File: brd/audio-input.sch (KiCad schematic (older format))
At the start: 15 parts, among them U6 MCP6004

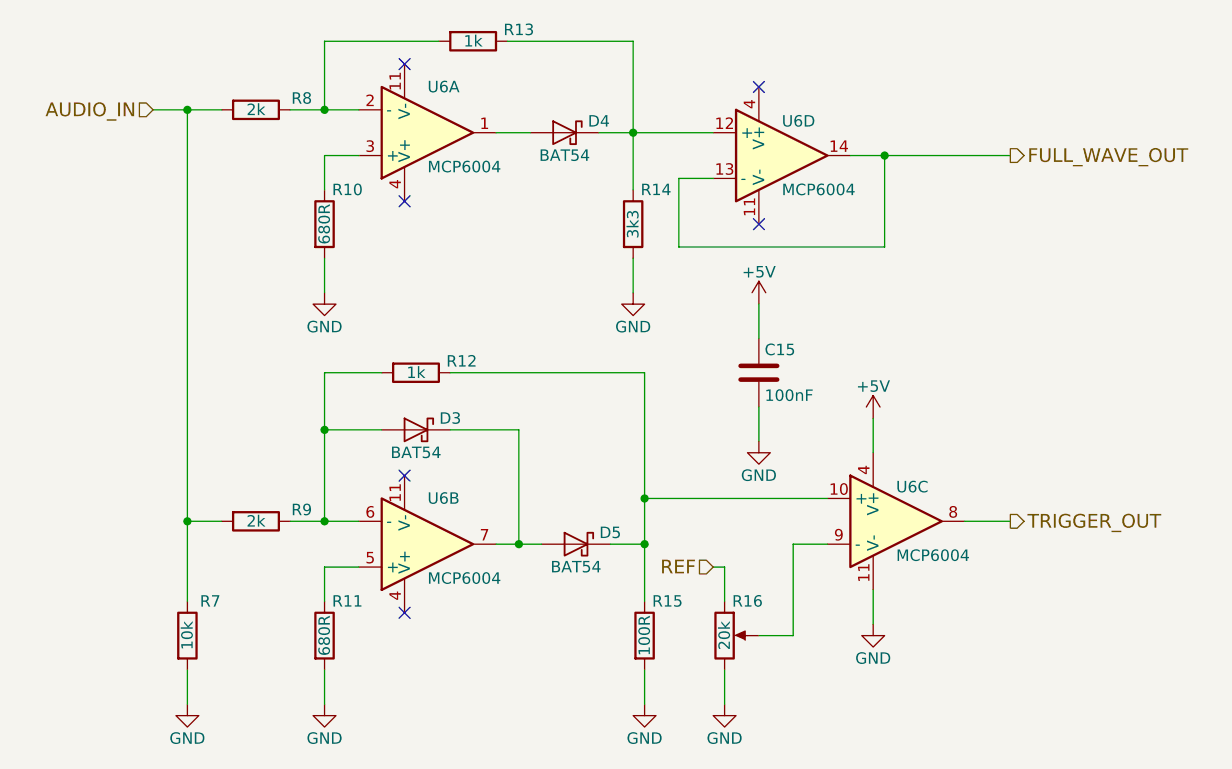
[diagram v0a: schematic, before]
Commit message: corregido problema con referencia analogica
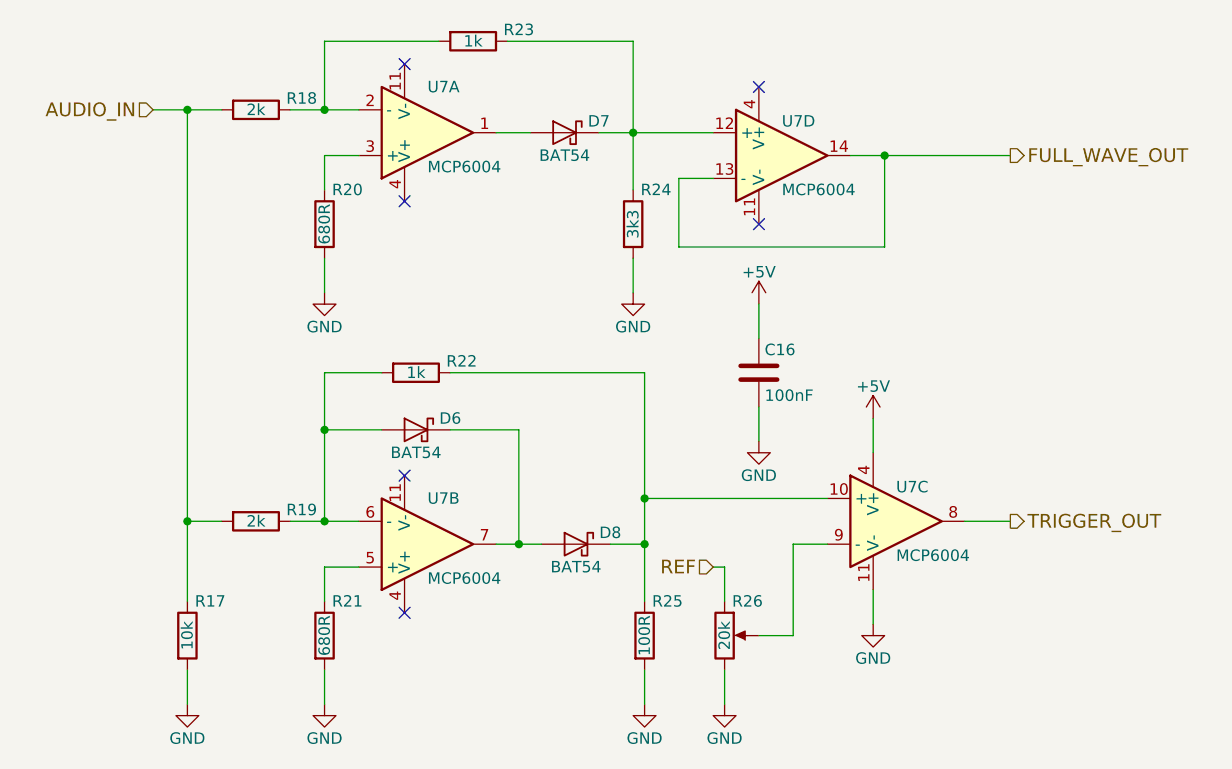
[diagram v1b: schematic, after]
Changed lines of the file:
@@
 AR Path="/5DA48168/5DA48258" Ref="U6"  Part="2"
 AR Path="/5DA4FC1E/5DA48258" Ref="U7"  Part="2"
-F 0 "U6" H 5050 4050 50  0000 L CNN
+F 0 "U7" H 5050 4050 50  0000 L CNN
 F 1 "MCP6004" H 5050 4400 50  0000 L CNN
 F 2 "Housings_SSOP:TSSOP-14_4.4x5mm_Pitch0.65mm" H 5000 4350 50  0001 C CNN
@@
 AR Path="/5DA48168/5DA482D7" Ref="R11"  Part="1"
 AR Path="/5DA4FC1E/5DA482D7" Ref="R21"  Part="1"
-F 0 "R11" H 4700 4800 50  0000 C CNN
+F 0 "R21" H 4700 4800 50  0000 C CNN
 F 1 "680R" V 4600 4650 50  0000 C CNN
 F 2 "Resistors_SMD:R_0805_HandSoldering" V 4530 4650 50  0001 C CNN
@@
 AR Path="/5DA48168/5DA48CC8" Ref="R15"  Part="1"
 AR Path="/5DA4FC1E/5DA48CC8" Ref="R25"  Part="1"
-F 0 "R15" H 6100 4800 50  0000 C CNN
+F 0 "R25" H 6100 4800 50  0000 C CNN
 F 1 "100R" V 6000 4650 50  0000 C CNN
 F 2 "Resistors_SMD:R_0805_HandSoldering" V 5930 4650 50  0001 C CNN
@@
 AR Path="/5DA48168/5DA48D92" Ref="R9"  Part="1"
 AR Path="/5DA4FC1E/5DA48D92" Ref="R19"  Part="1"
-F 0 "R9" V 4250 4350 50  0000 C CNN
+F 0 "R19" V 4250 4350 50  0000 C CNN
 F 1 "2k" V 4300 4150 50  0000 C CNN
 F 2 "Resistors_SMD:R_0805_HandSoldering" V 4230 4150 50  0001 C CNN
@@
 AR Path="/5DA48168/5DA48DF2" Ref="R12"  Part="1"
 AR Path="/5DA4FC1E/5DA48DF2" Ref="R22"  Part="1"
-F 0 "R12" V 4950 3700 50  0000 C CNN
+F 0 "R22" V 4950 3700 50  0000 C CNN
 F 1 "1k" V 5000 3500 50  0000 C CNN
 F 2 "Resistors_SMD:R_0805_HandSoldering" V 4930 3500 50  0001 C CNN
@@
 AR Path="/5DA48168/5DA49319" Ref="R7"  Part="1"
 AR Path="/5DA4FC1E/5DA49319" Ref="R17"  Part="1"
-F 0 "R7" H 4100 4800 50  0000 C CNN
+F 0 "R17" H 4100 4800 50  0000 C CNN
 F 1 "10k" V 4000 4650 50  0000 C CNN
 F 2 "Resistors_SMD:R_0805_HandSoldering" V 3930 4650 50  0001 C CNN
@@
 AR Path="/5DA48168/5DA496BC" Ref="U6"  Part="1"
 AR Path="/5DA4FC1E/5DA496BC" Ref="U7"  Part="1"
-F 0 "U6" H 5050 2250 50  0000 L CNN
+F 0 "U7" H 5050 2250 50  0000 L CNN
 F 1 "MCP6004" H 5050 2600 50  0000 L CNN
 F 2 "Housings_SSOP:TSSOP-14_4.4x5mm_Pitch0.65mm" H 5000 2550 50  0001 C CNN
@@
 AR Path="/5DA48168/5DA496C2" Ref="R10"  Part="1"
 AR Path="/5DA4FC1E/5DA496C2" Ref="R20"  Part="1"
-F 0 "R10" H 4700 3000 50  0000 C CNN
+F 0 "R20" H 4700 3000 50  0000 C CNN
 F 1 "680R" V 4600 2850 50  0000 C CNN
 F 2 "Resistors_SMD:R_0805_HandSoldering" V 4530 2850 50  0001 C CNN
@@
 AR Path="/5DA48168/5DA496C8" Ref="D4"  Part="1"
 AR Path="/5DA4FC1E/5DA496C8" Ref="D7"  Part="1"
-F 0 "D4" H 5500 2500 50  0000 C CNN
+F 0 "D7" H 5500 2500 50  0000 C CNN
 F 1 "BAT54" H 5650 2350 50  0000 C CNN
 F 2 "Diodes_SMD:D_SOD-123" H 5650 2450 50  0001 C CNN
@@
 AR Path="/5DA48168/5DA496D0" Ref="R14"  Part="1"
 AR Path="/5DA4FC1E/5DA496D0" Ref="R24"  Part="1"
-F 0 "R14" H 6050 3000 50  0000 C CNN
+F 0 "R24" H 6050 3000 50  0000 C CNN
 F 1 "3k3" V 5950 2850 50  0000 C CNN
 F 2 "Resistors_SMD:R_0805_HandSoldering" V 5880 2850 50  0001 C CNN
@@
 AR Path="/5DA48168/5DA496D6" Ref="R8"  Part="1"
 AR Path="/5DA4FC1E/5DA496D6" Ref="R18"  Part="1"
-F 0 "R8" V 4250 2550 50  0000 C CNN
+F 0 "R18" V 4250 2550 50  0000 C CNN
 F 1 "2k" V 4300 2350 50  0000 C CNN
 F 2 "Resistors_SMD:R_0805_HandSoldering" V 4230 2350 50  0001 C CNN
@@
 AR Path="/5DA48168/5DA496DC" Ref="R13"  Part="1"
 AR Path="/5DA4FC1E/5DA496DC" Ref="R23"  Part="1"
-F 0 "R13" V 5200 2250 50  0000 C CNN
+F 0 "R23" V 5200 2250 50  0000 C CNN
 F 1 "1k" V 5250 2050 50  0000 C CNN
 F 2 "Resistors_SMD:R_0805_HandSoldering" V 5180 2050 50  0001 C CNN
@@
 Connection ~ 4600 2350
 $Comp
-L GND #PWR043
+L GND #PWR47
 U 1 1 5DA49A66
 P 6000 4950
-AR Path="/5DA48168/5DA49A66" Ref="#PWR043"  Part="1"
-AR Path="/5DA4FC1E/5DA49A66" Ref="#PWR053"  Part="1"
-F 0 "#PWR043" H 6000 4700 50  0001 C CNN
+AR Path="/5DA48168/5DA49A66" Ref="#PWR47"  Part="1"
+AR Path="/5DA4FC1E/5DA49A66" Ref="#PWR57"  Part="1"
+F 0 "#PWR57" H 6000 4700 50  0001 C CNN
 F 1 "GND" H 6000 4800 50  0000 C CNN
 F 2 "" H 6000 4950 50  0001 C CNN
@@
 $EndComp
 $Comp
-L GND #PWR044
+L GND #PWR45
 U 1 1 5DA49B2E
 P 4600 4950
-AR Path="/5DA48168/5DA49B2E" Ref="#PWR044"  Part="1"
-AR Path="/5DA4FC1E/5DA49B2E" Ref="#PWR054"  Part="1"
-F 0 "#PWR044" H 4600 4700 50  0001 C CNN
+AR Path="/5DA48168/5DA49B2E" Ref="#PWR45"  Part="1"
+AR Path="/5DA4FC1E/5DA49B2E" Ref="#PWR55"  Part="1"
+F 0 "#PWR55" H 4600 4700 50  0001 C CNN
 F 1 "GND" H 4600 4800 50  0000 C CNN
 F 2 "" H 4600 4950 50  0001 C CNN
@@
 AR Path="/5DA48168/5DA49C44" Ref="U6"  Part="3"
 AR Path="/5DA4FC1E/5DA49C44" Ref="U7"  Part="3"
-F 0 "U6" H 7100 4300 50  0000 L CNN
+F 0 "U7" H 7100 4300 50  0000 L CNN
 F 1 "MCP6004" H 7100 4000 50  0000 L CNN
 F 2 "Housings_SSOP:TSSOP-14_4.4x5mm_Pitch0.65mm" H 7050 4250 50  0001 C CNN
@@
 AR Path="/5DA48168/5DA49DEC" Ref="R16"  Part="1"
 AR Path="/5DA4FC1E/5DA49DEC" Ref="R26"  Part="1"
-F 0 "R16" H 6450 4800 50  0000 C CNN
+F 0 "R26" H 6450 4800 50  0000 C CNN
 F 1 "20k" V 6350 4650 50  0000 C CNN
 F 2 "Potentiometers:Potentiometer_Trimmer_Bourns_3299P" H 6350 4650 50  0001 C CNN
@@
 $EndComp
 $Comp
-L GND #PWR045
+L GND #PWR52
 U 1 1 5DA49F10
 P 7000 4600
-AR Path="/5DA48168/5DA49F10" Ref="#PWR045"  Part="1"
-AR Path="/5DA4FC1E/5DA49F10" Ref="#PWR055"  Part="1"
-F 0 "#PWR045" H 7000 4350 50  0001 C CNN
+AR Path="/5DA48168/5DA49F10" Ref="#PWR52"  Part="1"
+AR Path="/5DA4FC1E/5DA49F10" Ref="#PWR62"  Part="1"
+F 0 "#PWR62" H 7000 4350 50  0001 C CNN
 F 1 "GND" H 7000 4450 50  0000 C CNN
 F 2 "" H 7000 4600 50  0001 C CNN
@@
 $EndComp
 $Comp
-L +5V #PWR046
+L +5V #PWR49
 U 1 1 5DA49F3D
 P 6500 3200
-AR Path="/5DA48168/5DA49F3D" Ref="#PWR046"  Part="1"
-AR Path="/5DA4FC1E/5DA49F3D" Ref="#PWR056"  Part="1"
-F 0 "#PWR046" H 6500 3050 50  0001 C CNN
+AR Path="/5DA48168/5DA49F3D" Ref="#PWR49"  Part="1"
+AR Path="/5DA4FC1E/5DA49F3D" Ref="#PWR59"  Part="1"
+F 0 "#PWR59" H 6500 3050 50  0001 C CNN
 F 1 "+5V" H 6500 3340 50  0000 C CNN
 F 2 "" H 6500 3200 50  0001 C CNN
@@
 AR Path="/5DA48168/5DA4A24A" Ref="U6"  Part="4"
 AR Path="/5DA4FC1E/5DA4A24A" Ref="U7"  Part="4"
-F 0 "U6" H 6600 2700 50  0000 L CNN
+F 0 "U7" H 6600 2700 50  0000 L CNN
 F 1 "MCP6004" H 6600 2400 50  0000 L CNN
 F 2 "Housings_SSOP:TSSOP-14_4.4x5mm_Pitch0.65mm" H 6550 2650 50  0001 C CNN
@@
 	6900 2550 7600 2550
 $Comp
-L GND #PWR047
+L GND #PWR46
 U 1 1 5DA4AA4B
 P 5950 3150
-AR Path="/5DA48168/5DA4AA4B" Ref="#PWR047"  Part="1"
-AR Path="/5DA4FC1E/5DA4AA4B" Ref="#PWR057"  Part="1"
-F 0 "#PWR047" H 5950 2900 50  0001 C CNN
+AR Path="/5DA48168/5DA4AA4B" Ref="#PWR46"  Part="1"
+AR Path="/5DA4FC1E/5DA4AA4B" Ref="#PWR56"  Part="1"
+F 0 "#PWR56" H 5950 2900 50  0001 C CNN
 F 1 "GND" H 5950 3000 50  0000 C CNN
 F 2 "" H 5950 3150 50  0001 C CNN
@@
 $EndComp
 $Comp
-L GND #PWR048
+L GND #PWR44
 U 1 1 5DA4AAEF
 P 4600 3150
-AR Path="/5DA48168/5DA4AAEF" Ref="#PWR048"  Part="1"
-AR Path="/5DA4FC1E/5DA4AAEF" Ref="#PWR058"  Part="1"
-F 0 "#PWR048" H 4600 2900 50  0001 C CNN
+AR Path="/5DA48168/5DA4AAEF" Ref="#PWR44"  Part="1"
+AR Path="/5DA4FC1E/5DA4AAEF" Ref="#PWR54"  Part="1"
+F 0 "#PWR54" H 4600 2900 50  0001 C CNN
 F 1 "GND" H 4600 3000 50  0000 C CNN
 F 2 "" H 4600 3150 50  0001 C CNN
@@
 	4600 3000 4600 3150
 $Comp
-L GND #PWR049
+L GND #PWR43
 U 1 1 5DA4B110
 P 4000 4950
-AR Path="/5DA48168/5DA4B110" Ref="#PWR049"  Part="1"
-AR Path="/5DA4FC1E/5DA4B110" Ref="#PWR059"  Part="1"
-F 0 "#PWR049" H 4000 4700 50  0001 C CNN
+AR Path="/5DA48168/5DA4B110" Ref="#PWR43"  Part="1"
+AR Path="/5DA4FC1E/5DA4B110" Ref="#PWR53"  Part="1"
+F 0 "#PWR53" H 4000 4700 50  0001 C CNN
 F 1 "GND" H 4000 4800 50  0000 C CNN
 F 2 "" H 4000 4950 50  0001 C CNN
@@
 	7000 3850 7000 3700
 $Comp
-L GND #PWR050
+L GND #PWR48
 U 1 1 5DA4CFC0
 P 6350 4950
-AR Path="/5DA48168/5DA4CFC0" Ref="#PWR050"  Part="1"
-AR Path="/5DA4FC1E/5DA4CFC0" Ref="#PWR060"  Part="1"
-F 0 "#PWR050" H 6350 4700 50  0001 C CNN
+AR Path="/5DA48168/5DA4CFC0" Ref="#PWR48"  Part="1"
+AR Path="/5DA4FC1E/5DA4CFC0" Ref="#PWR58"  Part="1"
+F 0 "#PWR58" H 6350 4700 50  0001 C CNN
 F 1 "GND" H 6350 4800 50  0000 C CNN
 F 2 "" H 6350 4950 50  0001 C CNN
@@
 AR Path="/5DA48168/5DA51ABC" Ref="C15"  Part="1"
 AR Path="/5DA4FC1E/5DA51ABC" Ref="C16"  Part="1"
-F 0 "C15" H 6525 3600 50  0000 L CNN
+F 0 "C16" H 6525 3600 50  0000 L CNN
 F 1 "100nF" H 6525 3400 50  0000 L CNN
 F 2 "Capacitors_SMD:C_0805" H 6538 3350 50  0001 C CNN
@@
 $EndComp
 $Comp
-L +5V #PWR051
+L +5V #PWR51
 U 1 1 5DA51BFC
 P 7000 3700
-AR Path="/5DA48168/5DA51BFC" Ref="#PWR051"  Part="1"
-AR Path="/5DA4FC1E/5DA51BFC" Ref="#PWR061"  Part="1"
-F 0 "#PWR051" H 7000 3550 50  0001 C CNN
+AR Path="/5DA48168/5DA51BFC" Ref="#PWR51"  Part="1"
+AR Path="/5DA4FC1E/5DA51BFC" Ref="#PWR61"  Part="1"
+F 0 "#PWR61" H 7000 3550 50  0001 C CNN
 F 1 "+5V" H 7000 3840 50  0000 C CNN
 F 2 "" H 7000 3700 50  0001 C CNN
@@
 $EndComp
 $Comp
-L GND #PWR052
+L GND #PWR50
 U 1 1 5DA51C4F
 P 6500 3800
-AR Path="/5DA48168/5DA51C4F" Ref="#PWR052"  Part="1"
-AR Path="/5DA4FC1E/5DA51C4F" Ref="#PWR062"  Part="1"
-F 0 "#PWR052" H 6500 3550 50  0001 C CNN
+AR Path="/5DA48168/5DA51C4F" Ref="#PWR50"  Part="1"
+AR Path="/5DA4FC1E/5DA51C4F" Ref="#PWR60"  Part="1"
+F 0 "#PWR60" H 6500 3550 50  0001 C CNN
 F 1 "GND" H 6500 3650 50  0000 C CNN
 F 2 "" H 6500 3800 50  0001 C CNN
@@
 AR Path="/5DA48168/5DA746D9" Ref="D3"  Part="1"
 AR Path="/5DA4FC1E/5DA746D9" Ref="D6"  Part="1"
-F 0 "D3" H 4850 3800 50  0000 C CNN
+F 0 "D6" H 4850 3800 50  0000 C CNN
 F 1 "BAT54" H 5000 3650 50  0000 C CNN
 F 2 "Diodes_SMD:D_SOD-123" H 5000 3750 50  0001 C CNN
@@
 AR Path="/5DA48168/5DA748E2" Ref="D5"  Part="1"
 AR Path="/5DA4FC1E/5DA748E2" Ref="D8"  Part="1"
-F 0 "D5" H 5550 4300 50  0000 C CNN
+F 0 "D8" H 5550 4300 50  0000 C CNN
 F 1 "BAT54" H 5700 4150 50  0000 C CNN
 F 2 "Diodes_SMD:D_SOD-123" H 5700 4250 50  0001 C CNN
